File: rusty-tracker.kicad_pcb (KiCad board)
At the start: 4 copper layers, 50 x 85 mm, 180 parts, among them J1 SIM8051-6-0-14-01-X, J2 USB_C_Receptacle_USB2.0, J3 NFC, J4 tag-connect-swd, J5 Battery Connector, Q1 BC846, Q2 BC846, SW1 SW_Push, T1 Tab, T2 Tab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

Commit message: KiCAD v7, 6 layer version
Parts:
- removed G***: LOGO, LOGO
- C17, C20: moved to F.Cu
- moved C26 13.4 mm to (152.3, 124.2)
- moved C47 4.81 mm to (126.6, 128.9), turned to 0 degrees
- moved C20 3.62 mm to (151.0, 125.6), turned to -90 degrees
- moved R37 2.11 mm to (128.4, 128.9), turned to 0 degrees
- moved C17 1.96 mm to (149.3, 124.5)
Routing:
- net /BTN: track 18.0 -> 21.3 mm
- net Net-(Q1-Pad3): track 2.60 -> 5.57 mm, vias 0 -> 2
- net Net-(Q2-Pad3): track 2.60 -> 4.72 mm, vias 0 -> 2
- net /NFC1: track 29.5 -> 28.0 mm, vias 1 -> 2
- net /CHG_TH2: track 14.1 -> 15.3 mm, vias 0 -> 2
- net /NFC2: track 28.6 -> 27.6 mm, vias 1 -> 2
- net Net-(D9-Pad1): track 7.78 -> 8.43 mm, vias 0 -> 2
- net +BATT: track 106.3 -> 105.6 mm, vias 10 -> 14
- net /SIM_RST_P: track 15.6 -> 16.1 mm, vias 0 -> 2
- net /SIM_RST: track 10.9 -> 11.4 mm, vias 0 -> 2
- net /SIM_IO: track 12.1 -> 12.4 mm, vias 0 -> 2
- net /SIM_CLK_P: track 30.0 -> 30.2 mm, vias 0 -> 2
- net unconnected-(U2-PadP2): track 0.00 -> 0.05 mm, vias 0 -> 1
- net unconnected-(U2-PadK2): track 0.00 -> 0.05 mm, vias 0 -> 1
- net unconnected-(U2-PadB17): track 0.00 -> 0.05 mm, vias 0 -> 1
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- added copper zone on In3.Cu, net GND
- added copper zone on In4.Cu, net GND
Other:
- copper layers 4 -> 6
- board text removed: "datbegrijpikniet"

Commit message: Added buzzer
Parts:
- added BZ1: Buzzer, buzzers:AST0927, F.Cu at (147.0, 101.8)
- added D10: 1N4148, passive:D_0402_DFN1006, F.Cu at (143.2, 107.9)
- added Q3: BC846, sot:SOT-323, F.Cu at (143.5, 110.0)
- added R38: 470, passive:R_0402, F.Cu at (144.1, 112.0)
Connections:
- U2 pad B17: unconnected-(U2-PadB17) -> /BUZ
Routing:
- net /BUZ: track 0.00 -> 30.6 mm, vias 0 -> 2
- net +BATT: track 105.6 -> 127.6 mm, vias 14 -> 16
- net Net-(BZ1-+): track 0.00 -> 8.16 mm, vias 0 -> 2
- net Net-(Q3-B): track 0.00 -> 1.38 mm
- net unconnected-(U2-PadB17): track 0.05 -> 0.00 mm, vias 1 -> 0
- net unconnected-(U2-P1.08-PadP2): track 0.05 -> 0.00 mm, vias 1 -> 0
- net unconnected-(U2-AIN3/P0.05-PadK2): track 0.05 -> 0.00 mm, vias 1 -> 0
- net GND: vias 1042 -> 1039

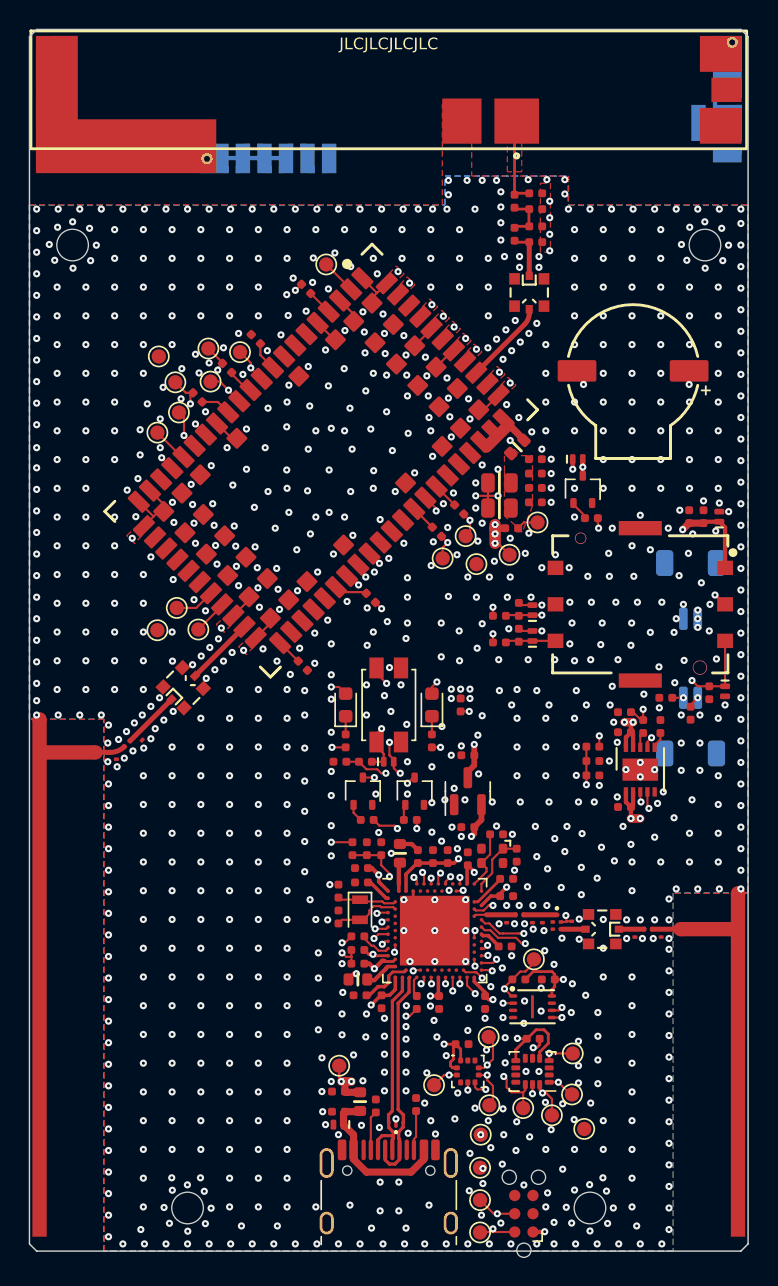
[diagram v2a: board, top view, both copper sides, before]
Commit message: Updated with buzzer and vibrator, removed voltage dividers
As they are available in the nRF52840 and charging IC
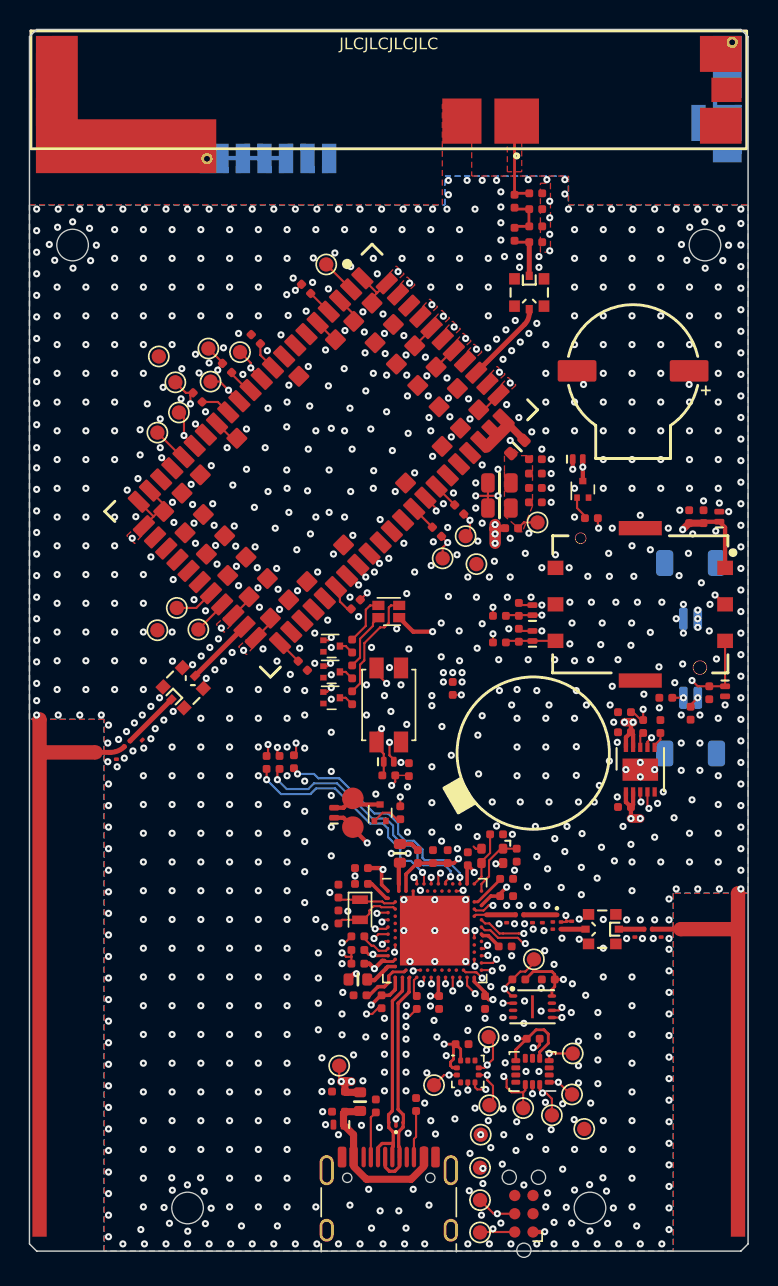
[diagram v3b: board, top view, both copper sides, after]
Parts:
- removed C12, C9: 0.1u, passive:C_0402
- removed C34, C46: 4.7u, passive:C_0402
- removed R17, R18, R19: 1 Meg, passive:R_0402
- removed R30: 100, passive:R_0402
- removed TP4: TestPoint, TestPoint:TestPoint_Pad_D1.0mm
- added J6: Conn_01x01, connectors:pad_circ_1.5mm, F.Cu at (127.5, 133.5)
- added J7: Conn_01x01, connectors:pad_circ_1.5mm, F.Cu at (127.5, 131.5)
- added Q4: RUM002N02T2L, Package_TO_SOT_SMD:SOT-723, F.Cu at (126.0, 120.9)
- added Q5: RUM002N02T2L, Package_TO_SOT_SMD:SOT-723, F.Cu at (129.4, 132.5)
- added R39: 150, passive:R_0402, F.Cu at (127.5, 120.9)
- added R40: 150, passive:R_0402, F.Cu at (127.5, 124.5)
- added R41: 100, passive:R_0402, F.Cu at (123.4, 128.9)
- D1: value GREEN -> 1N4148; footprint LED_SMD:LED_0603_1608Metric -> passive:D_0402_DFN1006
- D2: value RED -> LTST-C19HE1WT; footprint LED_SMD:LED_0603_1608Metric -> LED_SMD:LED_LiteOn_LTST-C19HE1WT
- Q1, Q2, Q3: value BC846 -> RUM002N02T2L; footprint sot:SOT-323 -> Package_TO_SOT_SMD:SOT-723
- R16: value 1 Meg -> 100
- R28, R32: value 5.1k -> 100
- R33: value 100 -> 150
- R35: value 69.8k -> 1.54k
- R36: value 1.54k -> 69.8k
- R38: value 470 -> 100
- U3: value DNP -> VC1034B018F; footprint Package_TO_SOT_SMD:SOT-23 -> vibrators:VC1034B018F
- moved R32 9.94 mm to (122.4, 129.0), turned to 90 degrees
- moved Q2 8.69 mm to (126.0, 124.5), turned to 0 degrees
- moved Q1 8.58 mm to (126.0, 122.7), turned to 0 degrees
- moved R28 8.06 mm to (121.5, 129.0), turned to 90 degrees
- moved D1 7.54 mm to (126.2, 132.5)
- moved R33 7.34 mm to (127.5, 122.7)
- moved D2 7.16 mm to (130.0, 118.5)
- moved U3 5.27 mm to (140.1, 128.3), turned to -60 degrees
- moved C47 4.83 mm to (131.4, 129.5), turned to -90 degrees
- moved R16 4.16 mm to (130.8, 132.5)
- moved R37 1.88 mm to (130.0, 129.9), turned to 180 degrees
- moved TH1 1.27 mm to (134.4, 123.8)
- moved R2 1.14 mm to (127.7, 118.0), turned to 45 degrees
- moved J2 0.50 mm to (130.0, 160.5)
- moved C39 0.10 mm to (128.1, 137.4)
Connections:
- D1 pad 1: Net-(D1-K) -> +BATT
- D1 pad 2: +BATT -> Net-(D1-A)
- D2 pad 2: +BATT -> Net-(D2-GK)
- Q1 pad 1: Net-(Q1-B) -> Net-(Q1-G)
- Q1 pad 3: Net-(Q1-C) -> /LED_RED
- Q2 pad 1: Net-(Q2-B) -> Net-(Q2-G)
- Q2 pad 3: Net-(Q2-C) -> /LED_BLUE
- R16 pad 1: VBUS -> /VIB
- R16 pad 2: /VUSB_MEAS -> Net-(Q5-G)
- R28 pad 2: Net-(Q1-B) -> Net-(Q4-G)
- R32 pad 2: Net-(Q2-B) -> Net-(Q1-G)
- R33 pad 2: Net-(Q2-C) -> /LED_RED
- U2 pad A10: /VUSB_MEAS -> /nRF52_GREEN
- U2 pad A12: /VBAT_MEAS -> /BUZ
- U2 pad A16: /nRF52_GREEN -> /nRF52_RED
- U2 pad A20: /nRF52_RED -> /nRF52_BLUE
- U2 pad B17: /BUZ -> unconnected-(U2-P1.12-PadB17)
- U2 pad B9: unconnected-(U2-AIN6/P0.30-PadB9) -> /VIB
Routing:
- net +BATT: track 127.6 -> 104.7 mm, vias 16 -> 15
- net /VBAT_MEAS: track 19.8 -> 0.00 mm, vias 2 -> 0
- net /BUZ: track 30.6 -> 47.6 mm
- net /nRF52_BLUE: track 0.00 -> 16.2 mm, vias 0 -> 2
- net /nRF52_RED: track 5.69 -> 17.6 mm
- net Net-(Q4-G): track 0.00 -> 11.4 mm, vias 0 -> 2
- net Net-(Q1-G): track 0.00 -> 9.10 mm, vias 0 -> 2
- net /nRF52_GREEN: track 7.75 -> 16.1 mm
- net /VIB: track 0.00 -> 8.13 mm, vias 0 -> 2
- net Net-(D2-BK): track 0.00 -> 7.84 mm
- net /VUSB_MEAS: track 7.74 -> 0.00 mm, vias 2 -> 0
- net Net-(Q2-G): track 0.00 -> 6.92 mm, vias 0 -> 2
- net Net-(Q1-C): track 5.57 -> 0.00 mm, vias 2 -> 0
- net Net-(Q2-C): track 4.72 -> 0.00 mm, vias 2 -> 0
- net +1V8: track 87.9 -> 83.5 mm, vias 12 -> 11
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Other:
- board text added: "+"
- board text added: "-"
- board text added: "VIB"

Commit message: Order sent to JLCPCB
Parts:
- J3: footprint Connector_JST:JST_SH_SM02B-SRSS-TB_1x02-1MP_P1.00mm_Horizontal -> Connector_FFC-FPC:TE_0-1734839-5_1x05-1MP_P0.5mm_Horizontal
- moved C17 4.40 mm to (152.5, 127.5), turned to 0 degrees
- moved C20 3.29 mm to (152.5, 128.5), turned to 0 degrees
- moved J3 1.50 mm to (151.0, 128.0), turned to 90 degrees
- moved R26 0.70 mm to (149.6, 126.5)
- moved C38 0.50 mm to (146.9, 132.1)
- moved C48 0.50 mm to (146.9, 126.9)
- moved R35 0.50 mm to (148.2, 126.5)
- moved R36 0.50 mm to (146.9, 125.5)
- moved U5 0.50 mm to (148.0, 129.5)
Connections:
- J3 pad 1: /NFC1 -> unconnected-(J3-Pin_1-Pad1)
- J3 pad 2: /NFC2 -> /NFC1
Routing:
- net /NFC1: track 28.0 -> 24.8 mm
- net /NFC2: track 27.6 -> 25.5 mm
- net /CHG_PG: track 21.4 -> 22.1 mm
- net +BATT: track 104.7 -> 104.0 mm
- net /BUZ: track 47.6 -> 48.1 mm
- net /CHG_TH2: track 15.5 -> 16.0 mm
- net /CHG_STAT2: track 18.2 -> 18.7 mm
- net /CHG_STAT1: track 17.4 -> 17.9 mm
- net GND: vias 1039 -> 1040

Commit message: Nicer text
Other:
- board text added: "GNSS TUNE"
- board text removed: "GPS TUNE"
